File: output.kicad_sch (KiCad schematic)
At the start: 103 parts, among them K1 G6K-2G-Y-TR_DC24_DPDT, K10 G6K-2G-Y-TR_DC24_DPDT, K11 G6K-2G-Y-TR_DC24_DPDT, K12 G6K-2G-Y-TR_DC24_DPDT, K13 G6K-2G-Y-TR_DC24_DPDT, K14 G6K-2G-Y-TR_DC24_DPDT, K15 G6K-2G-Y-TR_DC24_DPDT, K16 G6K-2G-Y-TR_DC24_DPDT, K2 G6K-2G-Y-TR_DC24_DPDT, K3 G6K-2G-Y-TR_DC24_DPDT, K4 G6K-2G-Y-TR_DC24_DPDT, K5 G6K-2G-Y-TR_DC24_DPDT, K6 G6K-2G-Y-TR_DC24_DPDT, K7 G6K-2G-Y-TR_DC24_DPDT, K8 G6K-2G-Y-TR_DC24_DPDT, K9 G6K-2G-Y-TR_DC24_DPDT, U14 ULN2803ADWR, U15 ULN2803ADWR, U5 TPS7B6950QDBVRQ1, U6 TLP290-4(TPE, U7 TLP290-4(TPE, U8 TLP290-4(TPE, U9 TLP290-4(TPE

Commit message: clean up
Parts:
- R139: symbol Resistor_Yageo:RC0603FR-07510KL -> Resistor_Yageo:RC0603FR-07510RL; ManufacturerPartNumber RC0603FR-07510KL -> RC0603FR-07510RL; Nominal 510k -> 510; Power (none) -> 1/10W; SupplierDevicePackage (none) -> R0603; SupplierPartNumber 311-510KHRTR-ND -> 311-510HRCT-ND

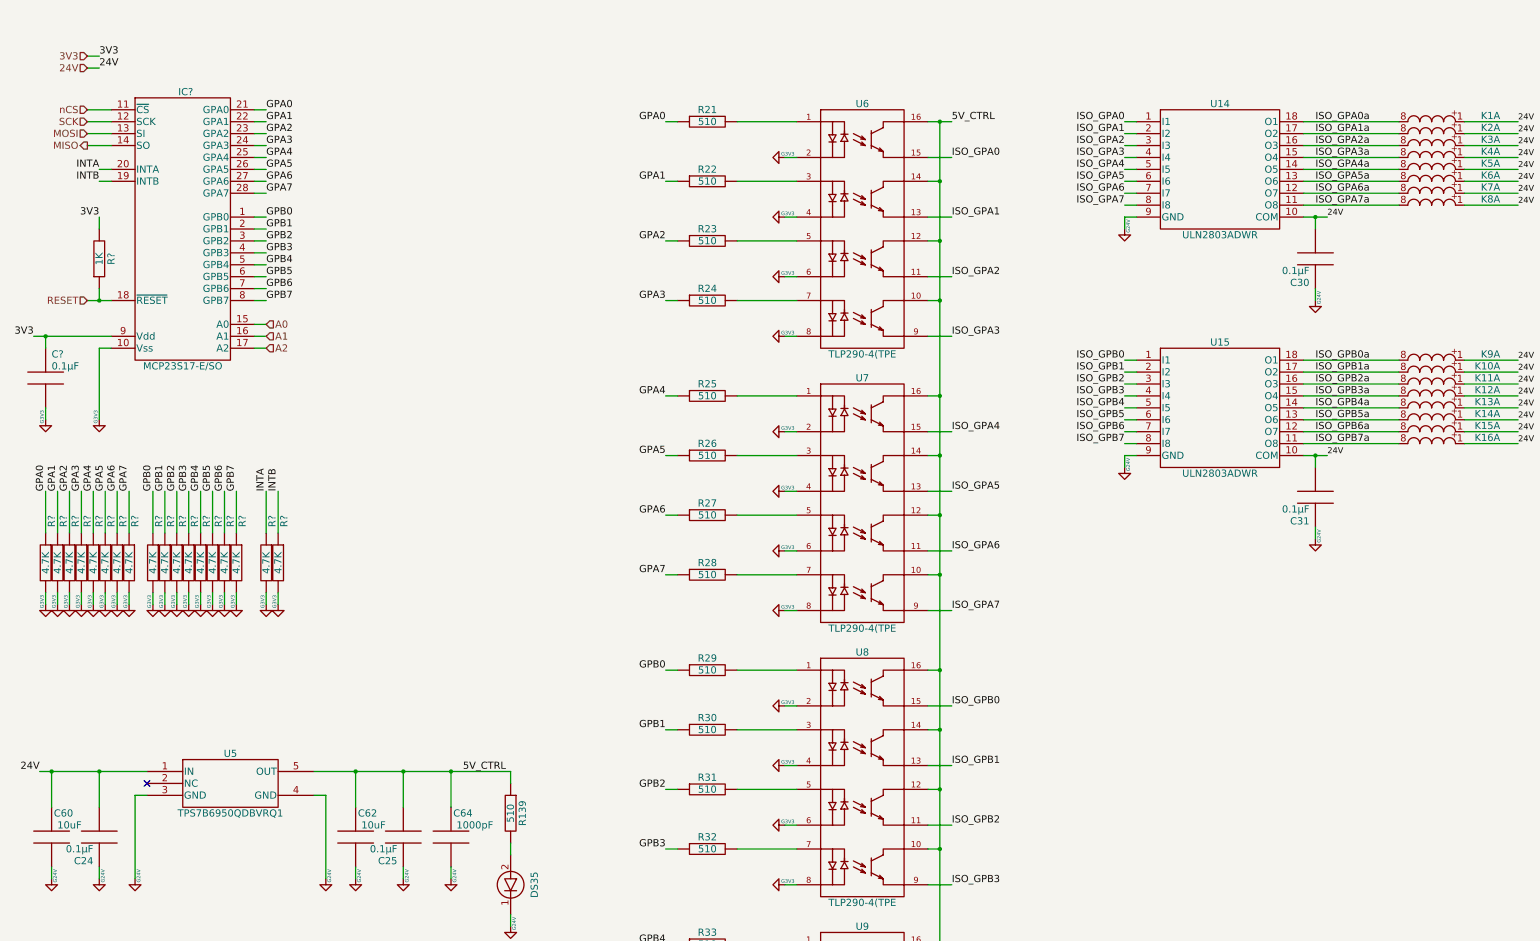
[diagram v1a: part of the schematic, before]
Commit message: kicad 9 - r11-check gerber before sending to manufacturing
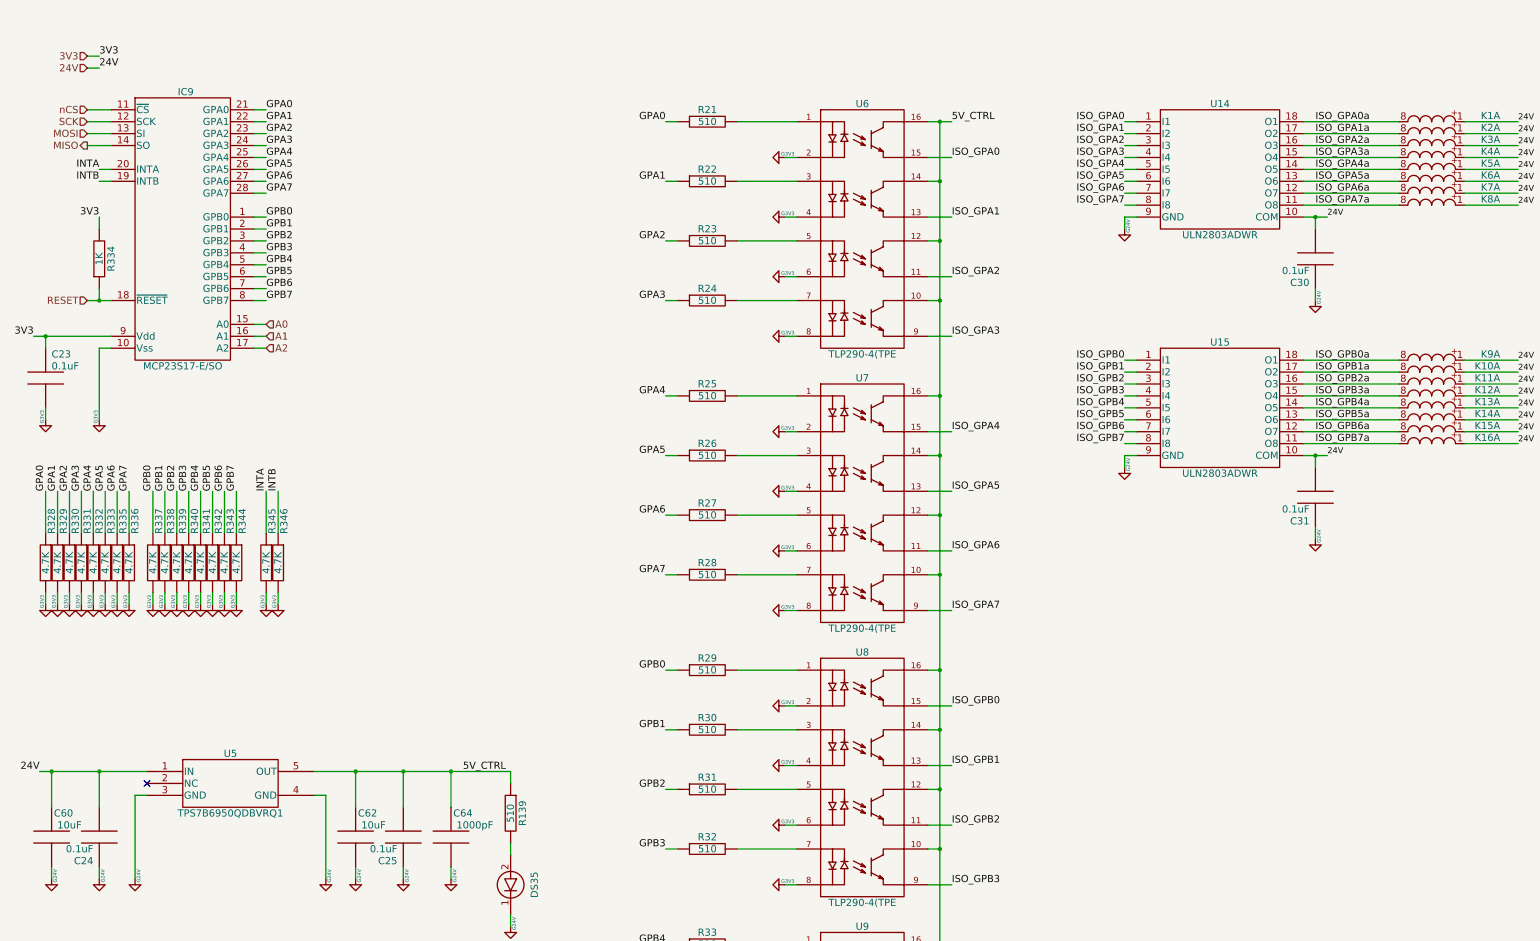
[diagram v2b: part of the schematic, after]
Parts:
- C23: renamed from C?; Nominal 0.1µF -> 0.1uF; SupllierPartNumber 478-3352-1-ND -> (none)
- C24, C25, C30, C31: Nominal 0.1µF -> 0.1uF
- DS10, DS11, DS12, DS13, DS14, DS15, DS16, DS17, DS18, DS3, DS4, DS5, DS6, DS7, DS8, DS9, R37, R38, R39, R40, R41, R42, R43, R44, R45, R46, R47, R48, R49, R50, R51, R52: fit_field DNP -> (none)
- IC9: renamed from IC?; SupllierPartNumber MCP23S17-E/SO-ND -> (none)
- MH1: renamed from MH3; now left out of the parts list
- MH2: renamed from MH4; now left out of the parts list
- R139: value RC0603FR-07510KL -> RC0603FR-07510RL
- R328, R329, R330, R331, R332, R333, R335, R336, R337, R338, R339, R340, R341, R342, R343, R344, R345, R346: renamed from R?; SupllierPartNumber 311-4.7KARCT-ND -> (none); Tolerance 5% -> (none)
- R334: renamed from R?; SupllierPartNumber 311-1.00KCRCT-ND -> (none); Tolerance 1% -> (none)
- U6, U7, U8, U9: footprint _SOIC_SOP:SOIC127P600X126-16 -> _SOIC_SOP:SOIC127P700X220-16
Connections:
- net GNDD renamed GND_3V3
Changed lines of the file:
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@@
-(kicad_sch (version 20230819) (generator eeschema)
-  (paper "A3")
-  (title_block
-    (title "EOL ECU MIX CARD")
-    (date "2023-09-26")
-    (rev "0C")
-    (company "ARXTRON TECHNOLOGIES")
-    (comment 1 "A0180-V0")
-    (comment 2 "PRJ22180")
-    (comment 3 "EOL ECU RCM8 RCM9")
-    (comment 4 "ANTON TOKARSKYI")
-  )
+(kicad_sch
+	(version 20250114)
+	(generator "eeschema")
+	(generator_version "9.0")
+	(paper "A3")
+	(title_block
+		(title "EOL ECU MIX CARD")
+		(date "2023-09-26")
+		(rev "0C")
+		(company "ARXTRON TECHNOLOGIES")
+		(comment 1 "A0180-V0")
+		(comment 2 "PRJ22180")
+		(comment 3 "EOL ECU RCM8 RCM9")
+		(comment 4 "ANTON TOKARSKYI")
+	)

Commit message: r11a - clean up mostly with reports naming, values, footprints and parts
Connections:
- net 24V: now also DS10.2 (-), DS11.2 (-), DS12.2 (-), DS13.2 (-), DS14.2 (-), DS15.2 (-), DS16.2 (-), DS17.2 (-), DS18.2 (-), DS3.2 (-), DS4.2 (-), DS5.2 (-), DS6.2 (-), DS7.2 (-), DS8.2 (-), DS9.2 (-)
- net GND_24V: no longer DS10.1 (+), DS11.1 (+), DS12.1 (+), DS13.1 (+), DS14.1 (+), DS15.1 (+), DS16.1 (+), DS17.1 (+), DS18.1 (+), DS3.1 (+), DS4.1 (+), DS5.1 (+), DS6.1 (+), DS7.1 (+), DS8.1 (+), DS9.1 (+)
- net at R49.2: now also DS15.1 (+); no longer DS15.2 (-)
- net at R52.2: now also DS18.1 (+); no longer DS18.2 (-)
- net at R51.2: now also DS17.1 (+); no longer DS17.2 (-)
- net at R46.2: now also DS12.1 (+); no longer DS12.2 (-)
- net at R42.2: now also DS8.1 (+); no longer DS8.2 (-)
- net at R48.2: now also DS14.1 (+); no longer DS14.2 (-)
- net at R43.2: now also DS9.1 (+); no longer DS9.2 (-)
- net at R38.2: now also DS4.1 (+); no longer DS4.2 (-)
- net at R41.2: now also DS7.1 (+); no longer DS7.2 (-)
- net at R37.2: now also DS3.1 (+); no longer DS3.2 (-)
- net at R45.2: now also DS11.1 (+); no longer DS11.2 (-)
- net at R47.2: now also DS13.1 (+); no longer DS13.2 (-)
- net at R40.2: now also DS6.1 (+); no longer DS6.2 (-)
- net at R50.2: now also DS16.1 (+); no longer DS16.2 (-)
- net at R44.2: now also DS10.1 (+); no longer DS10.2 (-)
- net at R39.2: now also DS5.1 (+); no longer DS5.2 (-)
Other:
- company: ARXTRON TECHNOLOGIES -> ${COMPANY}
- title: EOL ECU MIX CARD -> ${PART_NUM} ${PCB_NAME} ${ASSY_VARIANT} ${ASSY_NAME}
- moved on the sheet: DS10, DS11, DS12, DS13, DS14, DS15, DS16, DS17, DS18, DS3, DS4, DS5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
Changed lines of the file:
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@@
 	(paper "A3")
 	(title_block
-		(title "EOL ECU MIX CARD")
-		(date "2023-09-26")
-		(rev "0C")
-		(company "ARXTRON TECHNOLOGIES")
-		(comment 1 "A0180-V0")
-		(comment 2 "PRJ22180")
-		(comment 3 "EOL ECU RCM8 RCM9")
-		(comment 4 "ANTON TOKARSKYI")
+		(title "${PART_NUM} ${PCB_NAME} ${ASSY_VARIANT} ${ASSY_NAME}")
+		(date "2025-03-12")
+		(rev "${REVISION}${REVISION_SCH}")
+		(company "${COMPANY}")
+		(comment 1 "${PART_NUM}")
+		(comment 2 "${PRJ_NUM}")
+		(comment 3 "${PRJ_NAME}")
+		(comment 4 "${DESIGNED}")
+		(comment 5 "${PART_NUM_ICT}")
 	)

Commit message: r11a released with gerbers - uln updated, leds updated - still dnp
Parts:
- U14, U15: value ULN2803ADWR -> ULN2803CDWR; footprint _TI:SOIC127P1030X265-18 -> _TI:SOIC127P1030X265-20; symbol TI:ULN2803ADWR -> TI:ULN2803CDWR; ManufacturerPartNumber ULN2803ADWR -> ULN2803CDWR; SupplierDevicePackage 18-SOIC (0.295" 7.50mm Width) -> 20-SOIC (7.5W); SupplierPartNumber 296-15777-1-ND -> 296-ULN2803CDWRTR-ND
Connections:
- net 24V: now also U14.12 (COM), U15.12 (COM); no longer U14.10 (COM), U15.10 (COM)
- net ISO_GPA0a: now also U14.20 (1C); no longer U14.18 (O1)
- net ISO_GPA1a: now also U14.19 (2C); no longer U14.17 (O2)
- net ISO_GPA2a: now also U14.18 (3C); no longer U14.16 (O3)
- net ISO_GPA3a: now also U14.17 (4C); no longer U14.15 (O4)
- net ISO_GPA4a: now also U14.16 (5C); no longer U14.14 (O5)
- net ISO_GPA5a: now also U14.15 (6C); no longer U14.13 (O6)
- net ISO_GPA6a: now also U14.14 (7C); no longer U14.12 (O7)
- net ISO_GPA7a: now also U14.13 (8C); no longer U14.11 (O8)
- net ISO_GPB0a: now also U15.20 (1C); no longer U15.18 (O1)
- net ISO_GPB1a: now also U15.19 (2C); no longer U15.17 (O2)
- net ISO_GPB2a: now also U15.18 (3C); no longer U15.16 (O3)
- net ISO_GPB3a: now also U15.17 (4C); no longer U15.15 (O4)
- net ISO_GPB4a: now also U15.16 (5C); no longer U15.14 (O5)
- net ISO_GPB5a: now also U15.15 (6C); no longer U15.13 (O6)
- net ISO_GPB6a: now also U15.14 (7C); no longer U15.12 (O7)
- net ISO_GPB7a: now also U15.13 (8C); no longer U15.11 (O8)
- no-connect marks 1 -> 5
